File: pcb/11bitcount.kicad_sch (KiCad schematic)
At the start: 3 parts

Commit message: WIP schematic
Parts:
- gave numbers to parts that had none: 3
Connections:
- net VCC renamed +5V

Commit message: WIP PCB
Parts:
- renumbered U14 to U?, U12 to U?, U13 to U?
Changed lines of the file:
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@@
 		(shape input)
 		(at 109.22 39.37 90)
-		(fields_autoplaced yes)
 		(effects
 			(font
@@
 		(shape input)
 		(at 66.04 39.37 90)
-		(fields_autoplaced yes)
 		(effects
 			(font
@@
 		(shape output)
 		(at 114.3 90.17 270)
-		(fields_autoplaced yes)
 		(effects
 			(font
@@
 		(shape output)
 		(at 116.84 90.17 270)
-		(fields_autoplaced yes)
 		(effects
 			(font
@@
 		(shape input)
 		(at 149.86 39.37 90)
-		(fields_autoplaced yes)
 		(effects
 			(font
@@
 		(shape input)
 		(at 38.1 43.18 180)
-		(fields_autoplaced yes)
 		(effects
 			(font
@@
 		(shape output)
 		(at 66.04 90.17 270)
-		(fields_autoplaced yes)
 		(effects
 			(font
@@
 		(shape input)
 		(at 114.3 39.37 90)
-		(fields_autoplaced yes)
 		(effects
 			(font
@@
 		(shape output)
 		(at 60.96 90.17 270)
-		(fields_autoplaced yes)
 		(effects
 			(font
@@
 		(shape output)
 		(at 160.02 90.17 270)
-		(fields_autoplaced yes)
 		(effects
 			(font
@@
 		(shape input)
 		(at 165.1 39.37 90)
-		(fields_autoplaced yes)
 		(effects
 			(font
@@
 		(shape output)
 		(at 58.42 90.17 270)
-		(fields_autoplaced yes)
 		(effects
 			(font
@@
 		(shape output)
 		(at 111.76 90.17 270)
-		(fields_autoplaced yes)
 		(effects
 			(font
@@
 		(shape input)
 		(at 38.1 45.72 180)
-		(fields_autoplaced yes)
 		(effects
 			(font
@@
 		(shape input)
 		(at 111.76 39.37 90)
-		(fields_autoplaced yes)
 		(effects
 			(font
@@
 		(shape output)
 		(at 162.56 90.17 270)
-		(fields_autoplaced yes)
 		(effects
 			(font
@@
 		(shape input)
 		(at 63.5 39.37 90)
-		(fields_autoplaced yes)
 		(effects
 			(font
@@
 		(shape input)
 		(at 162.56 39.37 90)
-		(fields_autoplaced yes)
 		(effects
 			(font
@@
 		(shape output)
 		(at 165.1 90.17 270)
-		(fields_autoplaced yes)
 		(effects
 			(font
@@
 		(shape input)
 		(at 167.64 39.37 90)
-		(fields_autoplaced yes)
 		(effects
 			(font
@@
 		(shape input)
 		(at 160.02 39.37 90)
-		(fields_autoplaced yes)
 		(effects
 			(font
@@
 		(shape output)
 		(at 63.5 90.17 270)
-		(fields_autoplaced yes)
 		(effects
 			(font
@@
 		(shape output)
 		(at 109.22 90.17 270)
-		(fields_autoplaced yes)
 		(effects
 			(font
@@
 		(shape input)
 		(at 60.96 39.37 90)
-		(fields_autoplaced yes)
 		(effects
 			(font
@@
 		(shape output)
 		(at 167.64 90.17 270)
-		(fields_autoplaced yes)
 		(effects
 			(font
@@
 		(shape input)
 		(at 116.84 39.37 90)
-		(fields_autoplaced yes)
 		(effects
 			(font
@@
 		(dnp no)
 		(fields_autoplaced yes)
-		(property "Reference" "#PWR057"
+		(property "Reference" "#PWR?"
 			(at 83.82 77.47 0)
 			(effects
@@
 			(project ""
 				(path "/e63e39d7-6ac0-4ffd-8aa3-1841a4541b55/90e1f016-3c60-4383-aa8d-def9977ac47b/78a99c0a-f468-453e-aea1-d254ed568110"
-					(reference "#PWR057")
+					(reference "#PWR?")
 					(unit 1)
 				)
 				(path "/e63e39d7-6ac0-4ffd-8aa3-1841a4541b55/90e1f016-3c60-4383-aa8d-def9977ac47b/d909784a-ae31-4c8f-b386-03ea0f044fee"
-					(reference "#PWR066")
+					(reference "#PWR?")
 					(unit 1)
 				)
@@
 		(dnp no)
 		(fields_autoplaced yes)
-		(property "Reference" "#PWR055"
+		(property "Reference" "#PWR?"
 			(at 58.42 43.18 0)
 			(effects
@@
 			(project ""
 				(path "/e63e39d7-6ac0-4ffd-8aa3-1841a4541b55/90e1f016-3c60-4383-aa8d-def9977ac47b/78a99c0a-f468-453e-aea1-d254ed568110"
-					(reference "#PWR055")
+					(reference "#PWR?")
 					(unit 1)
 				)
 				(path "/e63e39d7-6ac0-4ffd-8aa3-1841a4541b55/90e1f016-3c60-4383-aa8d-def9977ac47b/d909784a-ae31-4c8f-b386-03ea0f044fee"
-					(reference "#PWR064")
+					(reference "#PWR?")
 					(unit 1)
 				)
@@
 		(on_board yes)
 		(dnp no)
-		(property "Reference" "U14"
+		(property "Reference" "U?"
 			(at 142.748 76.708 90)
 			(effects
@@
 			(project ""
 				(path "/e63e39d7-6ac0-4ffd-8aa3-1841a4541b55/90e1f016-3c60-4383-aa8d-def9977ac47b/78a99c0a-f468-453e-aea1-d254ed568110"
-					(reference "U14")
+					(reference "U?")
 					(unit 1)
 				)
 				(path "/e63e39d7-6ac0-4ffd-8aa3-1841a4541b55/90e1f016-3c60-4383-aa8d-def9977ac47b/d909784a-ae31-4c8f-b386-03ea0f044fee"
-					(reference "U17")
+					(reference "U?")
 					(unit 1)
 				)
@@
 		(dnp no)
 		(fields_autoplaced yes)
-		(property "Reference" "#PWR060"
+		(property "Reference" "#PWR?"
 			(at 134.62 77.47 0)
 			(effects
@@
 			(project ""
 				(path "/e63e39d7-6ac0-4ffd-8aa3-1841a4541b55/90e1f016-3c60-4383-aa8d-def9977ac47b/78a99c0a-f468-453e-aea1-d254ed568110"
-					(reference "#PWR060")
+					(reference "#PWR?")
 					(unit 1)
 				)
 				(path "/e63e39d7-6ac0-4ffd-8aa3-1841a4541b55/90e1f016-3c60-4383-aa8d-def9977ac47b/d909784a-ae31-4c8f-b386-03ea0f044fee"
-					(reference "#PWR069")
+					(reference "#PWR?")
 					(unit 1)
 				)
@@
 		(dnp no)
 		(fields_autoplaced yes)
-		(property "Reference" "#PWR056"
+		(property "Reference" "#PWR?"
 			(at 73.66 74.93 0)
 			(effects
@@
 			(project ""
 				(path "/e63e39d7-6ac0-4ffd-8aa3-1841a4541b55/90e1f016-3c60-4383-aa8d-def9977ac47b/78a99c0a-f468-453e-aea1-d254ed568110"
-					(reference "#PWR056")
+					(reference "#PWR?")
 					(unit 1)
 				)
 				(path "/e63e39d7-6ac0-4ffd-8aa3-1841a4541b55/90e1f016-3c60-4383-aa8d-def9977ac47b/d909784a-ae31-4c8f-b386-03ea0f044fee"
-					(reference "#PWR065")
+					(reference "#PWR?")
 					(unit 1)
 				)
@@
 		(dnp no)
 		(fields_autoplaced yes)
-		(property "Reference" "#PWR061"
+		(property "Reference" "#PWR?"
 			(at 152.4 43.18 0)
 			(effects
@@
 			(project ""
 				(path "/e63e39d7-6ac0-4ffd-8aa3-1841a4541b55/90e1f016-3c60-4383-aa8d-def9977ac47b/78a99c0a-f468-453e-aea1-d254ed568110"
-					(reference "#PWR061")
+					(reference "#PWR?")
 					(unit 1)
 				)
 				(path "/e63e39d7-6ac0-4ffd-8aa3-1841a4541b55/90e1f016-3c60-4383-aa8d-def9977ac47b/d909784a-ae31-4c8f-b386-03ea0f044fee"
-					(reference "#PWR070")
+					(reference "#PWR?")
 					(unit 1)
 				)
@@
 		(dnp no)
 		(fields_autoplaced yes)
-		(property "Reference" "#PWR054"
+		(property "Reference" "#PWR?"
 			(at 33.02 77.47 0)
 			(effects
@@
 			(project ""
 				(path "/e63e39d7-6ac0-4ffd-8aa3-1841a4541b55/90e1f016-3c60-4383-aa8d-def9977ac47b/78a99c0a-f468-453e-aea1-d254ed568110"
-					(reference "#PWR054")
+					(reference "#PWR?")
 					(unit 1)
 				)
 				(path "/e63e39d7-6ac0-4ffd-8aa3-1841a4541b55/90e1f016-3c60-4383-aa8d-def9977ac47b/d909784a-ae31-4c8f-b386-03ea0f044fee"
-					(reference "#PWR063")
+					(reference "#PWR?")
 					(unit 1)
 				)
@@
 		(dnp no)
 		(fields_autoplaced yes)
-		(property "Reference" "#PWR058"
+		(property "Reference" "#PWR?"
 			(at 99.06 43.18 0)
 			(effects
@@
 			(project ""
 				(path "/e63e39d7-6ac0-4ffd-8aa3-1841a4541b55/90e1f016-3c60-4383-aa8d-def9977ac47b/78a99c0a-f468-453e-aea1-d254ed568110"
-					(reference "#PWR058")
+					(reference "#PWR?")
 					(unit 1)
 				)
 				(path "/e63e39d7-6ac0-4ffd-8aa3-1841a4541b55/90e1f016-3c60-4383-aa8d-def9977ac47b/d909784a-ae31-4c8f-b386-03ea0f044fee"
-					(reference "#PWR067")
+					(reference "#PWR?")
 					(unit 1)
 				)
@@
 		(on_board yes)
 		(dnp no)
-		(property "Reference" "U12"
+		(property "Reference" "U?"
 			(at 41.148 76.708 90)
 			(effects
@@
 			(project "fnx51"
 				(path "/e63e39d7-6ac0-4ffd-8aa3-1841a4541b55/90e1f016-3c60-4383-aa8d-def9977ac47b/78a99c0a-f468-453e-aea1-d254ed568110"
-					(reference "U12")
+					(reference "U?")
 					(unit 1)
 				)
 				(path "/e63e39d7-6ac0-4ffd-8aa3-1841a4541b55/90e1f016-3c60-4383-aa8d-def9977ac47b/d909784a-ae31-4c8f-b386-03ea0f044fee"
-					(reference "U15")
+					(reference "U?")
 					(unit 1)
 				)
@@
 		(on_board yes)
 		(dnp no)
-		(property "Reference" "U13"
+		(property "Reference" "U?"
 			(at 91.948 76.708 90)
 			(effects
@@
 			(project "fnx51"
 				(path "/e63e39d7-6ac0-4ffd-8aa3-1841a4541b55/90e1f016-3c60-4383-aa8d-def9977ac47b/78a99c0a-f468-453e-aea1-d254ed568110"
-					(reference "U13")
+					(reference "U?")
 					(unit 1)
 				)
 				(path "/e63e39d7-6ac0-4ffd-8aa3-1841a4541b55/90e1f016-3c60-4383-aa8d-def9977ac47b/d909784a-ae31-4c8f-b386-03ea0f044fee"
-					(reference "U16")
+					(reference "U?")
 					(unit 1)
 				)
@@
 		(dnp no)
 		(fields_autoplaced yes)
-		(property "Reference" "#PWR062"
+		(property "Reference" "#PWR?"
 			(at 175.26 74.93 0)
 			(effects
@@
 			(project ""
 				(path "/e63e39d7-6ac0-4ffd-8aa3-1841a4541b55/90e1f016-3c60-4383-aa8d-def9977ac47b/78a99c0a-f468-453e-aea1-d254ed568110"
-					(reference "#PWR062")
+					(reference "#PWR?")
 					(unit 1)
 				)
 				(path "/e63e39d7-6ac0-4ffd-8aa3-1841a4541b55/90e1f016-3c60-4383-aa8d-def9977ac47b/d909784a-ae31-4c8f-b386-03ea0f044fee"
-					(reference "#PWR071")
+					(reference "#PWR?")
 					(unit 1)
 				)
@@
 		(dnp no)
 		(fields_autoplaced yes)
-		(property "Reference" "#PWR059"
+		(property "Reference" "#PWR?"
 			(at 124.46 74.93 0)
 			(effects
@@
 			(project ""
 				(path "/e63e39d7-6ac0-4ffd-8aa3-1841a4541b55/90e1f016-3c60-4383-aa8d-def9977ac47b/78a99c0a-f468-453e-aea1-d254ed568110"
-					(reference "#PWR059")
+					(reference "#PWR?")
 					(unit 1)
 				)
 				(path "/e63e39d7-6ac0-4ffd-8aa3-1841a4541b55/90e1f016-3c60-4383-aa8d-def9977ac47b/d909784a-ae31-4c8f-b386-03ea0f044fee"
-					(reference "#PWR068")
-					(unit 1)
-				)
+					(reference "#PWR?")
+					(unit 1)
+				)

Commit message: wip schematic
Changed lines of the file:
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@@
 		(on_board yes)
 		(dnp no)
-		(fields_autoplaced yes)
 		(property "Reference" "#PWR?"
 			(at 58.42 43.18 0)
@@
 		)
 		(property "Value" "+5V"
-			(at 60.96 38.0999 0)
+			(at 54.61 34.29 0)
 			(effects
 				(font
@@
 		(on_board yes)
 		(dnp no)
-		(fields_autoplaced yes)
 		(property "Reference" "#PWR?"
 			(at 73.66 74.93 0)
@@
 		)
 		(property "Value" "+5V"
-			(at 76.2 69.8499 0)
+			(at 71.12 66.04 0)
 			(effects
 				(font
@@
 		(on_board yes)
 		(dnp no)
-		(fields_autoplaced yes)
 		(property "Reference" "#PWR?"
 			(at 152.4 43.18 0)
@@
 		)
 		(property "Value" "+5V"
-			(at 154.94 38.0999 0)
+			(at 149.86 34.29 0)
 			(effects
 				(font
@@
 		(on_board yes)
 		(dnp no)
-		(fields_autoplaced yes)
 		(property "Reference" "#PWR?"
 			(at 99.06 43.18 0)
@@
 		)
 		(property "Value" "+5V"
-			(at 101.6 38.0999 0)
+			(at 96.52 34.29 0)
 			(effects
 				(font
@@
 		(on_board yes)
 		(dnp no)
-		(fields_autoplaced yes)
 		(property "Reference" "#PWR?"
 			(at 175.26 74.93 0)
@@
 		)
 		(property "Value" "+5V"
-			(at 177.8 69.8499 0)
+			(at 172.72 66.04 0)
 			(effects
 				(font
@@
 		(on_board yes)
 		(dnp no)
-		(fields_autoplaced yes)
 		(property "Reference" "#PWR?"
 			(at 124.46 74.93 0)
@@
 		)
 		(property "Value" "+5V"
-			(at 127 69.8499 0)
-			(effects
-				(font
+			(at 121.92 66.04 0)
+			(effects
+				(font

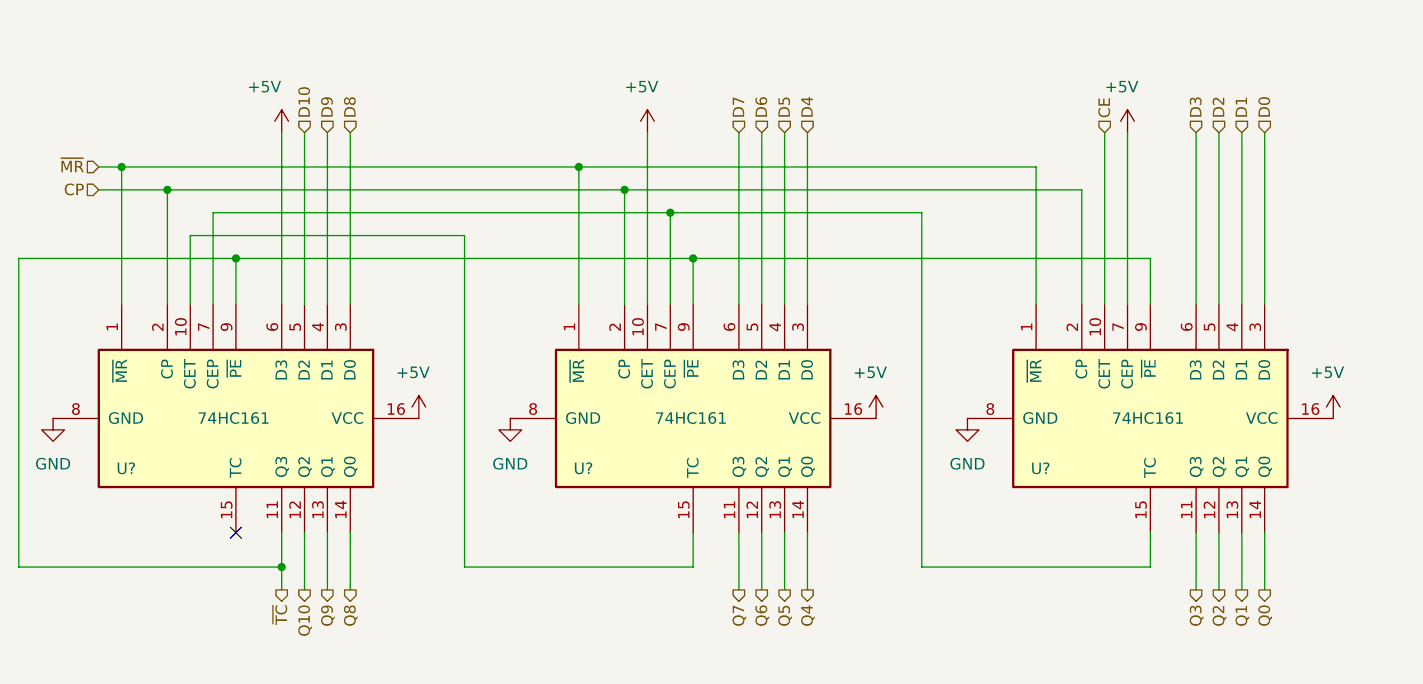
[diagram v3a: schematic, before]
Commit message: PCB: add reset circuit, xtal
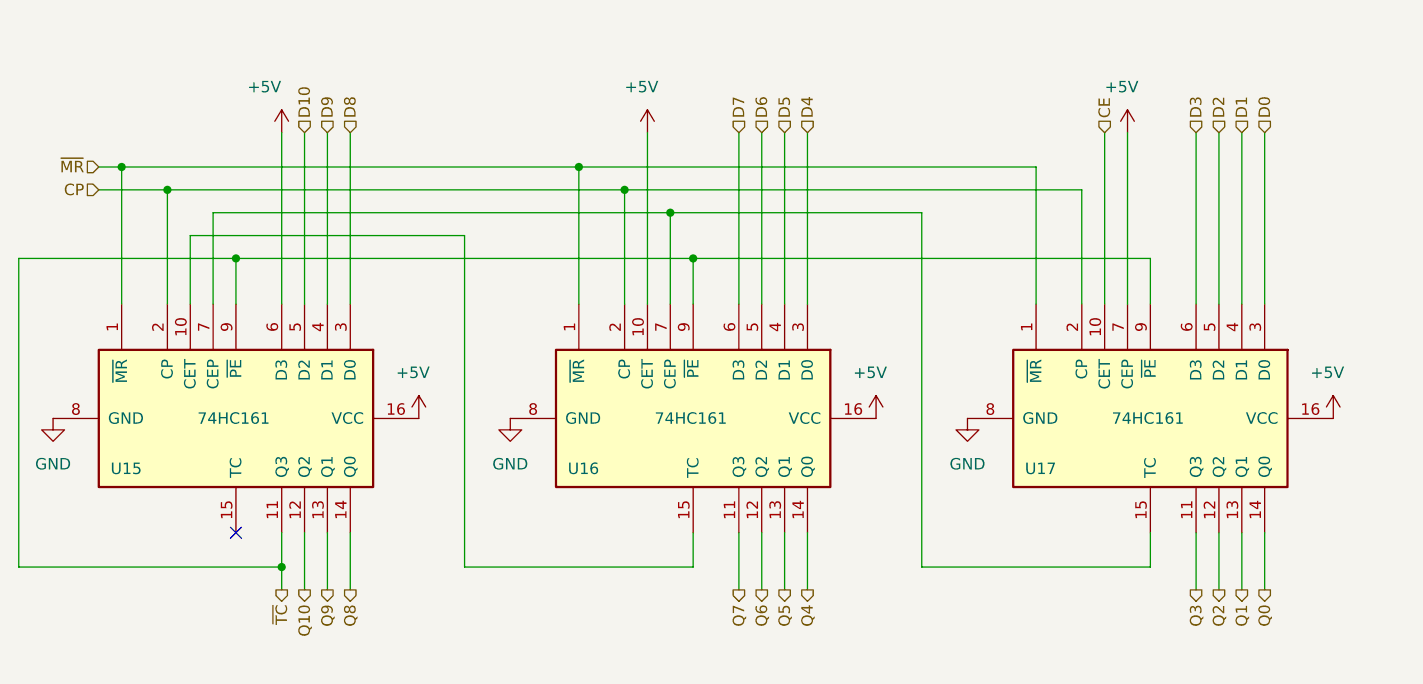
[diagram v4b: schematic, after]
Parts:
- gave numbers to parts that had none: 3
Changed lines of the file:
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@@
 (kicad_sch
-	(version 20231120)
+	(version 20250114)
 	(generator "eeschema")
-	(generator_version "8.0")
+	(generator_version "9.0")
 	(paper "A5")
 	(junction
@@
 		(dnp no)
 		(fields_autoplaced yes)
-		(property "Reference" "#PWR?"
+		(property "Reference" "#PWR070"
 			(at 83.82 77.47 0)
 			(effects
@@
 			(project ""
 				(path "/e63e39d7-6ac0-4ffd-8aa3-1841a4541b55/90e1f016-3c60-4383-aa8d-def9977ac47b/78a99c0a-f468-453e-aea1-d254ed568110"
-					(reference "#PWR?")
+					(reference "#PWR070")
 					(unit 1)
 				)
 				(path "/e63e39d7-6ac0-4ffd-8aa3-1841a4541b55/90e1f016-3c60-4383-aa8d-def9977ac47b/d909784a-ae31-4c8f-b386-03ea0f044fee"
-					(reference "#PWR?")
+					(reference "#PWR079")
 					(unit 1)
 				)
@@
 		(on_board yes)
 		(dnp no)
-		(property "Reference" "#PWR?"
+		(property "Reference" "#PWR068"
 			(at 58.42 43.18 0)
 			(effects
@@
 			(project ""
 				(path "/e63e39d7-6ac0-4ffd-8aa3-1841a4541b55/90e1f016-3c60-4383-aa8d-def9977ac47b/78a99c0a-f468-453e-aea1-d254ed568110"
-					(reference "#PWR?")
+					(reference "#PWR068")
 					(unit 1)
 				)
 				(path "/e63e39d7-6ac0-4ffd-8aa3-1841a4541b55/90e1f016-3c60-4383-aa8d-def9977ac47b/d909784a-ae31-4c8f-b386-03ea0f044fee"
-					(reference "#PWR?")
+					(reference "#PWR077")
 					(unit 1)
 				)
@@
 		(on_board yes)
 		(dnp no)
-		(property "Reference" "U?"
+		(property "Reference" "U17"
 			(at 142.748 76.708 90)
 			(effects
@@
 			(project ""
 				(path "/e63e39d7-6ac0-4ffd-8aa3-1841a4541b55/90e1f016-3c60-4383-aa8d-def9977ac47b/78a99c0a-f468-453e-aea1-d254ed568110"
-					(reference "U?")
+					(reference "U17")
 					(unit 1)
 				)
 				(path "/e63e39d7-6ac0-4ffd-8aa3-1841a4541b55/90e1f016-3c60-4383-aa8d-def9977ac47b/d909784a-ae31-4c8f-b386-03ea0f044fee"
-					(reference "U?")
+					(reference "U20")
 					(unit 1)
 				)
@@
 		(dnp no)
 		(fields_autoplaced yes)
-		(property "Reference" "#PWR?"
+		(property "Reference" "#PWR073"
 			(at 134.62 77.47 0)
 			(effects
@@
 			(project ""
 				(path "/e63e39d7-6ac0-4ffd-8aa3-1841a4541b55/90e1f016-3c60-4383-aa8d-def9977ac47b/78a99c0a-f468-453e-aea1-d254ed568110"
-					(reference "#PWR?")
+					(reference "#PWR073")
 					(unit 1)
 				)
 				(path "/e63e39d7-6ac0-4ffd-8aa3-1841a4541b55/90e1f016-3c60-4383-aa8d-def9977ac47b/d909784a-ae31-4c8f-b386-03ea0f044fee"
-					(reference "#PWR?")
+					(reference "#PWR082")
 					(unit 1)
 				)
@@
 		(on_board yes)
 		(dnp no)
-		(property "Reference" "#PWR?"
+		(property "Reference" "#PWR069"
 			(at 73.66 74.93 0)
 			(effects
@@
 			(project ""
 				(path "/e63e39d7-6ac0-4ffd-8aa3-1841a4541b55/90e1f016-3c60-4383-aa8d-def9977ac47b/78a99c0a-f468-453e-aea1-d254ed568110"
-					(reference "#PWR?")
+					(reference "#PWR069")
 					(unit 1)
 				)
 				(path "/e63e39d7-6ac0-4ffd-8aa3-1841a4541b55/90e1f016-3c60-4383-aa8d-def9977ac47b/d909784a-ae31-4c8f-b386-03ea0f044fee"
-					(reference "#PWR?")
+					(reference "#PWR078")
 					(unit 1)
 				)
@@
 		(on_board yes)
 		(dnp no)
-		(property "Reference" "#PWR?"
+		(property "Reference" "#PWR074"
 			(at 152.4 43.18 0)
 			(effects
@@
 			(project ""
 				(path "/e63e39d7-6ac0-4ffd-8aa3-1841a4541b55/90e1f016-3c60-4383-aa8d-def9977ac47b/78a99c0a-f468-453e-aea1-d254ed568110"
-					(reference "#PWR?")
+					(reference "#PWR074")
 					(unit 1)
 				)
 				(path "/e63e39d7-6ac0-4ffd-8aa3-1841a4541b55/90e1f016-3c60-4383-aa8d-def9977ac47b/d909784a-ae31-4c8f-b386-03ea0f044fee"
-					(reference "#PWR?")
+					(reference "#PWR083")
 					(unit 1)
 				)
@@
 		(dnp no)
 		(fields_autoplaced yes)
-		(property "Reference" "#PWR?"
+		(property "Reference" "#PWR067"
 			(at 33.02 77.47 0)
 			(effects
@@
 			(project ""
 				(path "/e63e39d7-6ac0-4ffd-8aa3-1841a4541b55/90e1f016-3c60-4383-aa8d-def9977ac47b/78a99c0a-f468-453e-aea1-d254ed568110"
-					(reference "#PWR?")
+					(reference "#PWR067")
 					(unit 1)
 				)
 				(path "/e63e39d7-6ac0-4ffd-8aa3-1841a4541b55/90e1f016-3c60-4383-aa8d-def9977ac47b/d909784a-ae31-4c8f-b386-03ea0f044fee"
-					(reference "#PWR?")
+					(reference "#PWR076")
 					(unit 1)
 				)
@@
 		(on_board yes)
 		(dnp no)
-		(property "Reference" "#PWR?"
+		(property "Reference" "#PWR071"
 			(at 99.06 43.18 0)
 			(effects
@@
 			(project ""
 				(path "/e63e39d7-6ac0-4ffd-8aa3-1841a4541b55/90e1f016-3c60-4383-aa8d-def9977ac47b/78a99c0a-f468-453e-aea1-d254ed568110"
-					(reference "#PWR?")
+					(reference "#PWR071")
 					(unit 1)
 				)
 				(path "/e63e39d7-6ac0-4ffd-8aa3-1841a4541b55/90e1f016-3c60-4383-aa8d-def9977ac47b/d909784a-ae31-4c8f-b386-03ea0f044fee"
-					(reference "#PWR?")
+					(reference "#PWR080")
 					(unit 1)
 				)
@@
 		(on_board yes)
 		(dnp no)
-		(property "Reference" "U?"
+		(property "Reference" "U15"
 			(at 41.148 76.708 90)
 			(effects
@@
 			(project "fnx51"
 				(path "/e63e39d7-6ac0-4ffd-8aa3-1841a4541b55/90e1f016-3c60-4383-aa8d-def9977ac47b/78a99c0a-f468-453e-aea1-d254ed568110"
-					(reference "U?")
+					(reference "U15")
 					(unit 1)
 				)
 				(path "/e63e39d7-6ac0-4ffd-8aa3-1841a4541b55/90e1f016-3c60-4383-aa8d-def9977ac47b/d909784a-ae31-4c8f-b386-03ea0f044fee"
-					(reference "U?")
+					(reference "U18")
 					(unit 1)
 				)
@@
 		(on_board yes)
 		(dnp no)
-		(property "Reference" "U?"
+		(property "Reference" "U16"
 			(at 91.948 76.708 90)
 			(effects
@@
 			(project "fnx51"
 				(path "/e63e39d7-6ac0-4ffd-8aa3-1841a4541b55/90e1f016-3c60-4383-aa8d-def9977ac47b/78a99c0a-f468-453e-aea1-d254ed568110"
-					(reference "U?")
+					(reference "U16")
 					(unit 1)
 				)
 				(path "/e63e39d7-6ac0-4ffd-8aa3-1841a4541b55/90e1f016-3c60-4383-aa8d-def9977ac47b/d909784a-ae31-4c8f-b386-03ea0f044fee"
-					(reference "U?")
+					(reference "U19")
 					(unit 1)
 				)
@@
 		(on_board yes)
 		(dnp no)
-		(property "Reference" "#PWR?"
+		(property "Reference" "#PWR075"
 			(at 175.26 74.93 0)
 			(effects
@@
 			(project ""
 				(path "/e63e39d7-6ac0-4ffd-8aa3-1841a4541b55/90e1f016-3c60-4383-aa8d-def9977ac47b/78a99c0a-f468-453e-aea1-d254ed568110"
-					(reference "#PWR?")
+					(reference "#PWR075")
 					(unit 1)
 				)
 				(path "/e63e39d7-6ac0-4ffd-8aa3-1841a4541b55/90e1f016-3c60-4383-aa8d-def9977ac47b/d909784a-ae31-4c8f-b386-03ea0f044fee"
-					(reference "#PWR?")
+					(reference "#PWR084")
 					(unit 1)
 				)
@@
 		(on_board yes)
 		(dnp no)
-		(property "Reference" "#PWR?"
+		(property "Reference" "#PWR072"
 			(at 124.46 74.93 0)
 			(effects
@@
 			(project ""
 				(path "/e63e39d7-6ac0-4ffd-8aa3-1841a4541b55/90e1f016-3c60-4383-aa8d-def9977ac47b/78a99c0a-f468-453e-aea1-d254ed568110"
-					(reference "#PWR?")
+					(reference "#PWR072")
 					(unit 1)
 				)
 				(path "/e63e39d7-6ac0-4ffd-8aa3-1841a4541b55/90e1f016-3c60-4383-aa8d-def9977ac47b/d909784a-ae31-4c8f-b386-03ea0f044fee"
-					(reference "#PWR?")
-					(unit 1)
-				)
+					(reference "#PWR081")
+					(unit 1)
+				)
